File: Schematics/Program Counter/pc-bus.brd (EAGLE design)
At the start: 133.3 x 152.1 mm, 22 parts

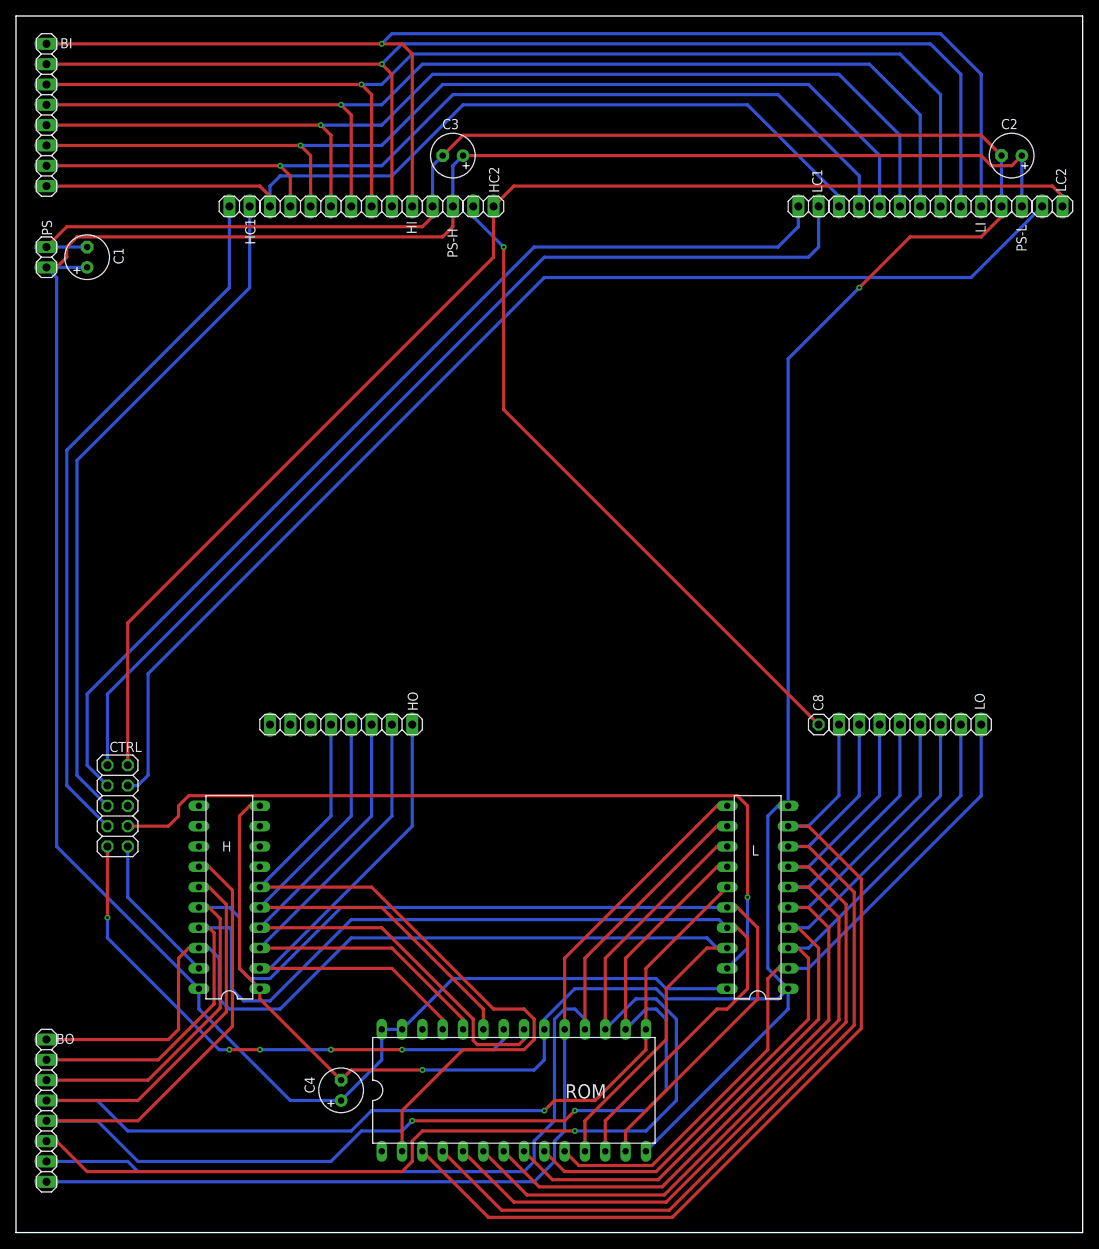
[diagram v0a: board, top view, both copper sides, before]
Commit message: Fixed DIR pin on HOE and LOE. Found when I was testing real brd.
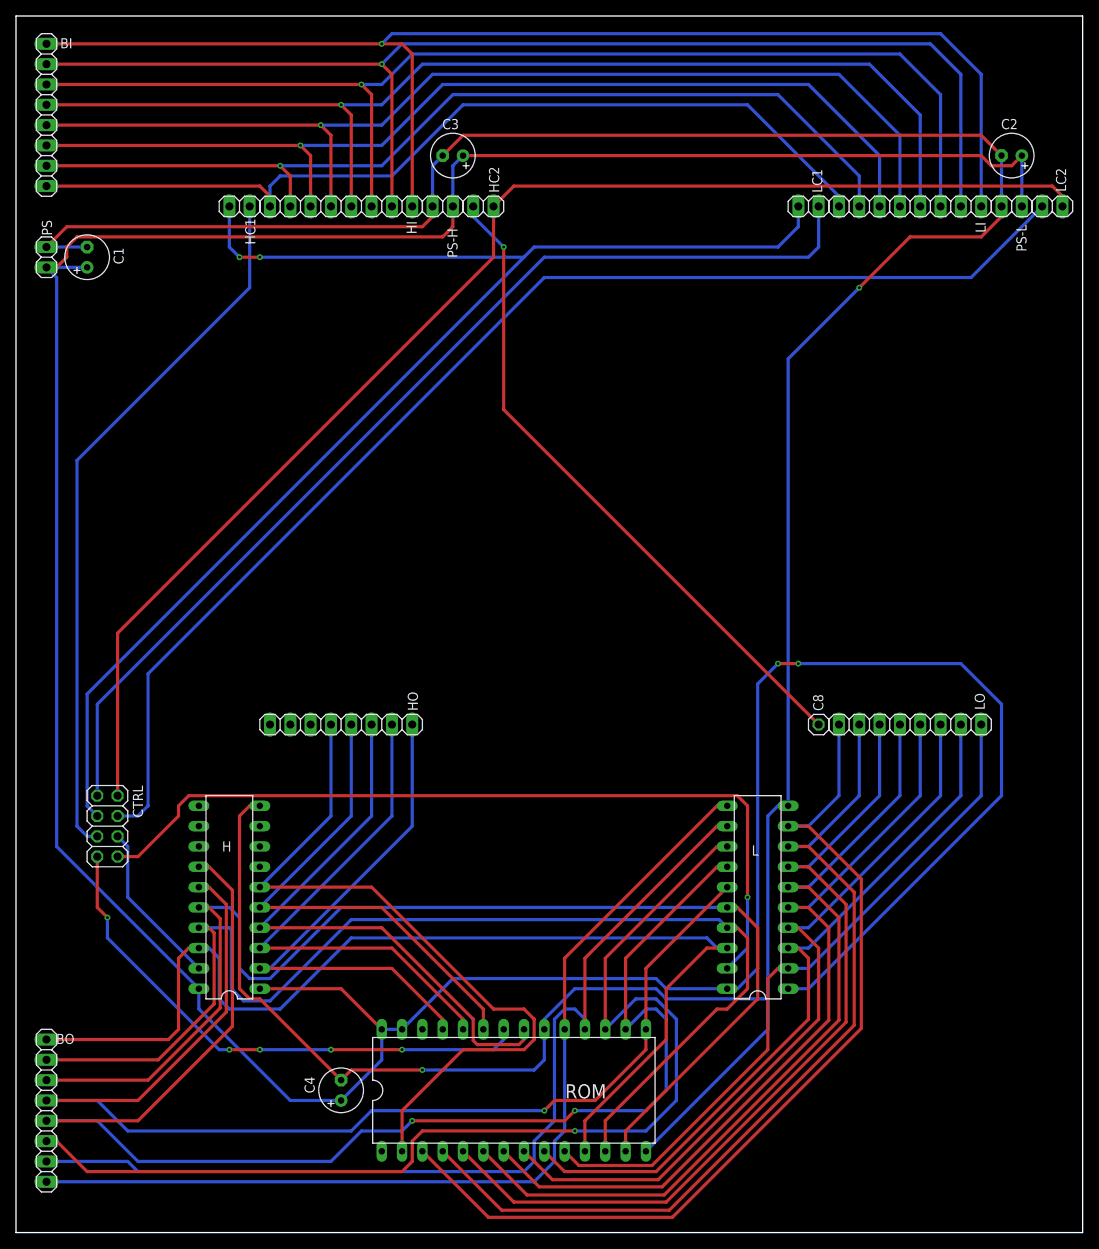
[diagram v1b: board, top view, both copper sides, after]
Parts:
- CTRL: device pinhead:2X05 -> pinhead:2X04
- moved CTRL 2.84 mm to (11.4, 50.8)
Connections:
- removed net HLD: CTRL.7, HC1.1
- removed net N$5: CTRL.6
- net GND: no longer H.1, L.1
- net HOE: now also CTRL.6; no longer CTRL.10
- net LLD: now also HC1.1
- net OE: now also CTRL.7; no longer CTRL.9
- net VCC: now also H.1, L.1
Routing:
- net VCC: track 325.8 -> 465.3 mm, vias 0 -> 2
- net HLD: track 88.0 -> 0.00 mm
- net LLD: track 128.1 -> 173.8 mm, vias 0 -> 2
- net INC: track 151.7 -> 156.8 mm
- net GND: track 391.9 -> 387.5 mm
- net LCP: track 126.0 -> 130.4 mm
- net CLR: track 162.8 -> 167.1 mm
- net HCP: track 85.5 -> 89.5 mm
- net LOE: track 101.7 -> 104.5 mm
- net HOE: track 18.9 -> 20.7 mm
- net O7: track 120.0 -> 118.7 mm
- net OE: track 68.5 -> 67.8 mm
